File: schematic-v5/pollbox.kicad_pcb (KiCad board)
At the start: 2 copper layers, 50.8 x 74.9 mm, 24 parts, among them P1 CONN_01X15, P10 CONN_01X04, P2 CONN_02X03, P20 CONN_01X04, P3 CONN_01X15, P30 CONN_01X04, P40 CONN_01X04, P50 CONN_01X04, U1 NodeMCU, U2 ULN2803

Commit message: o Completing routing of board v5.
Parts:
- removed W1, W2, W3, W4: TEST_1P, Connect:1pin
- added HOLE1: MountingHole_3.2mm_M3, Mounting_Holes.pretty:MountingHole_3.2mm_M3, F.Cu at (82.5, 52.1)
- added HOLE2: MountingHole_3.2mm_M3, Mounting_Holes.pretty:MountingHole_3.2mm_M3, F.Cu at (123.2, 52.1)
- added HOLE3: MountingHole_3.2mm_M3, Mounting_Holes.pretty:MountingHole_3.2mm_M3, F.Cu at (123.2, 106.7)
- added HOLE4: MountingHole_3.2mm_M3, Mounting_Holes.pretty:MountingHole_3.2mm_M3, F.Cu at (82.5, 106.7)
- U1: value NodeMCU -> NodeMCU_1.0; footprint nodemcu:NodeMCU_wide_2 -> nodemcu:NodeMCU
- U2: footprint Housings_DIP:DIP-18_W7.62mm -> Housings_DIP.pretty:DIP-18_W7.62mm_LongPads
- moved P1 35.7 mm to (121.9, 116.8), turned to 270 degrees
- moved P3 35.6 mm to (121.9, 86.4), turned to 270 degrees
- moved U1 24.4 mm to (105.4, 101.6)
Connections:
- P1 pad 13: (no net) -> Net-(P1-Pad13)
- P1 pad 14: (no net) -> Net-(P1-Pad14)
- P1 pad 5: (no net) -> Net-(P1-Pad5)
- P1 pad 6: (no net) -> Net-(P1-Pad6)
- P3 pad 10: (no net) -> Net-(P3-Pad10)
- P3 pad 3: (no net) -> Net-(P3-Pad3)
- P3 pad 9: (no net) -> Net-(P3-Pad9)
- U1 pad 13: (no net) -> Net-(U1-Pad13)
- U1 pad 14: (no net) -> Net-(U1-Pad14)
- U1 pad 21: (no net) -> Net-(U1-Pad21)
- U1 pad 22: (no net) -> Net-(U1-Pad22)
- U1 pad 28: (no net) -> Net-(U1-Pad28)
- U1 pad 5: (no net) -> Net-(U1-Pad5)
- U1 pad 6: (no net) -> Net-(U1-Pad6)
- U2 pad 11: (no net) -> Net-(U2-Pad11)
- U2 pad 12: (no net) -> Net-(U2-Pad12)
- U2 pad 13: (no net) -> Net-(U2-Pad13)
- U2 pad 6: (no net) -> Net-(U2-Pad6)
- U2 pad 7: (no net) -> Net-(U2-Pad7)
- U2 pad 8: (no net) -> Net-(U2-Pad8)
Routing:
- net (no net): track 73.5 -> 0.00 mm
- net +5V: track 55.9 -> 112.4 mm
- net /SWITCH_4: track 12.9 -> 51.9 mm
- net /SWITCH_5: track 20.3 -> 55.8 mm
- net /SWITCH_3: track 11.5 -> 45.8 mm
- net GND: track 146.8 -> 179.3 mm
- net /SWITCH_2: track 11.8 -> 36.5 mm
- net /LED_5: track 1.27 -> 13.5 mm
- net /LED_2_OUT: track 0.90 -> 11.3 mm
- net /SWITCH_1: track 26.9 -> 36.6 mm
- net /LED_4_OUT: track 8.94 -> 17.1 mm
- net /LED_5_OUT: track 14.0 -> 21.9 mm
- net /LED_1: track 4.49 -> 9.94 mm
- net +3V3: track 159.7 -> 165.1 mm
- net /LED_1_OUT: track 8.26 -> 12.0 mm
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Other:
- net class narrow added: clearance 0.254, trace_width 0.3048, via_dia 0.6, via_drill 0.4

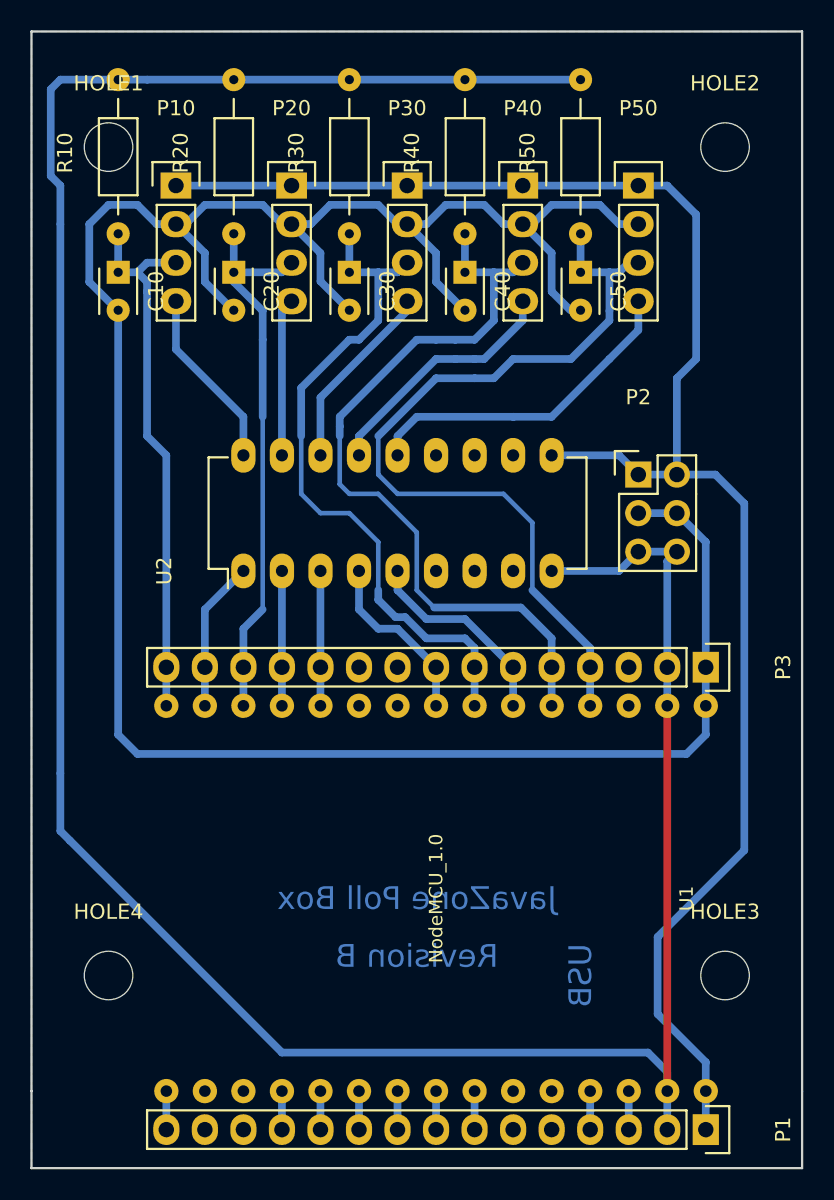
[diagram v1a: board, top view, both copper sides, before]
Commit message: rewire d0 and d1
To enable interrupt on button
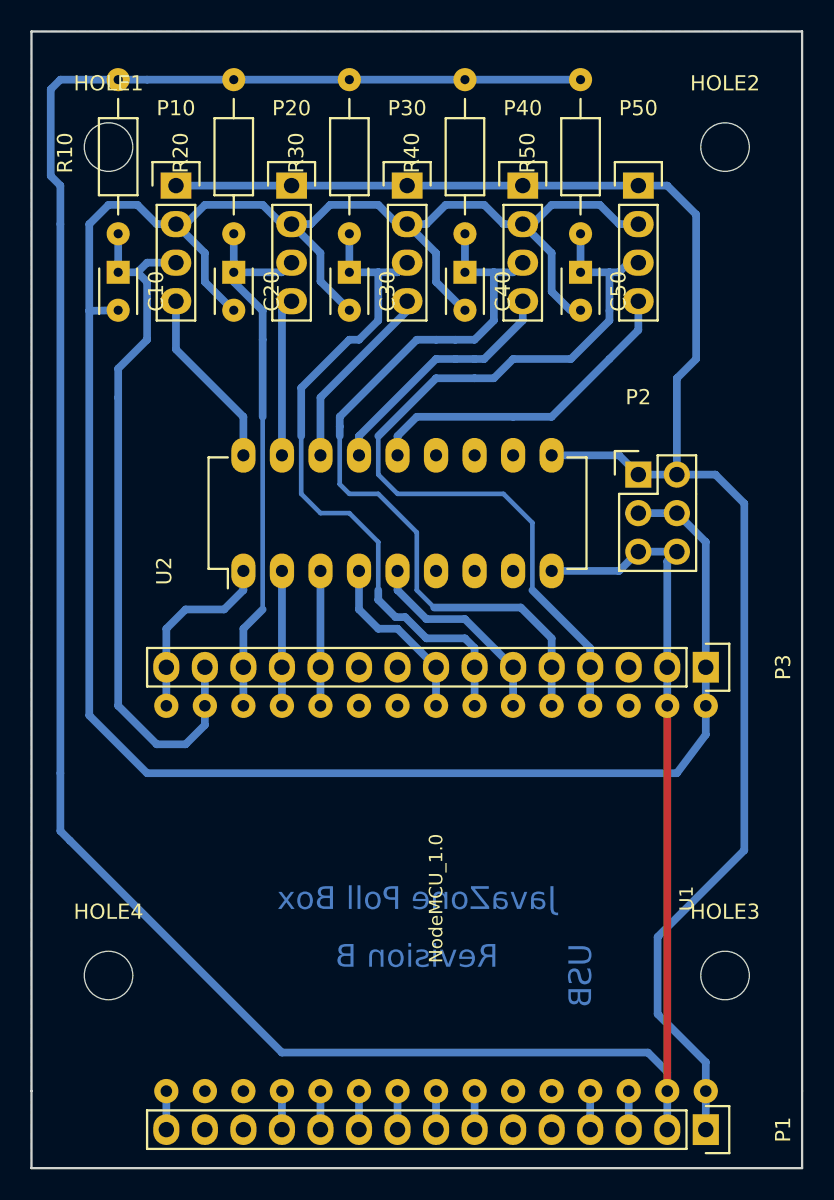
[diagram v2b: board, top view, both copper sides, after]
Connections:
- C10 pad 1: /SWITCH_1 -> /LED_1
- P10 pad 3: /SWITCH_1 -> /LED_1
- P3 pad 15: /SWITCH_1 -> Net-(P3-Pad15)
- R10 pad 1: /SWITCH_1 -> /LED_1
- U1 pad 16: /SWITCH_1 -> Net-(P3-Pad15)
- U2 pad 1: /LED_1 -> Net-(P3-Pad15)
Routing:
- net /LED_1: track 9.94 -> 48.0 mm
- net /SWITCH_1: track 36.6 -> 0.00 mm
- net Net-(P3-Pad15): track 0.00 -> 12.5 mm
- net +3V3: track 165.1 -> 168.6 mm

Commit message: cleanup some tracks
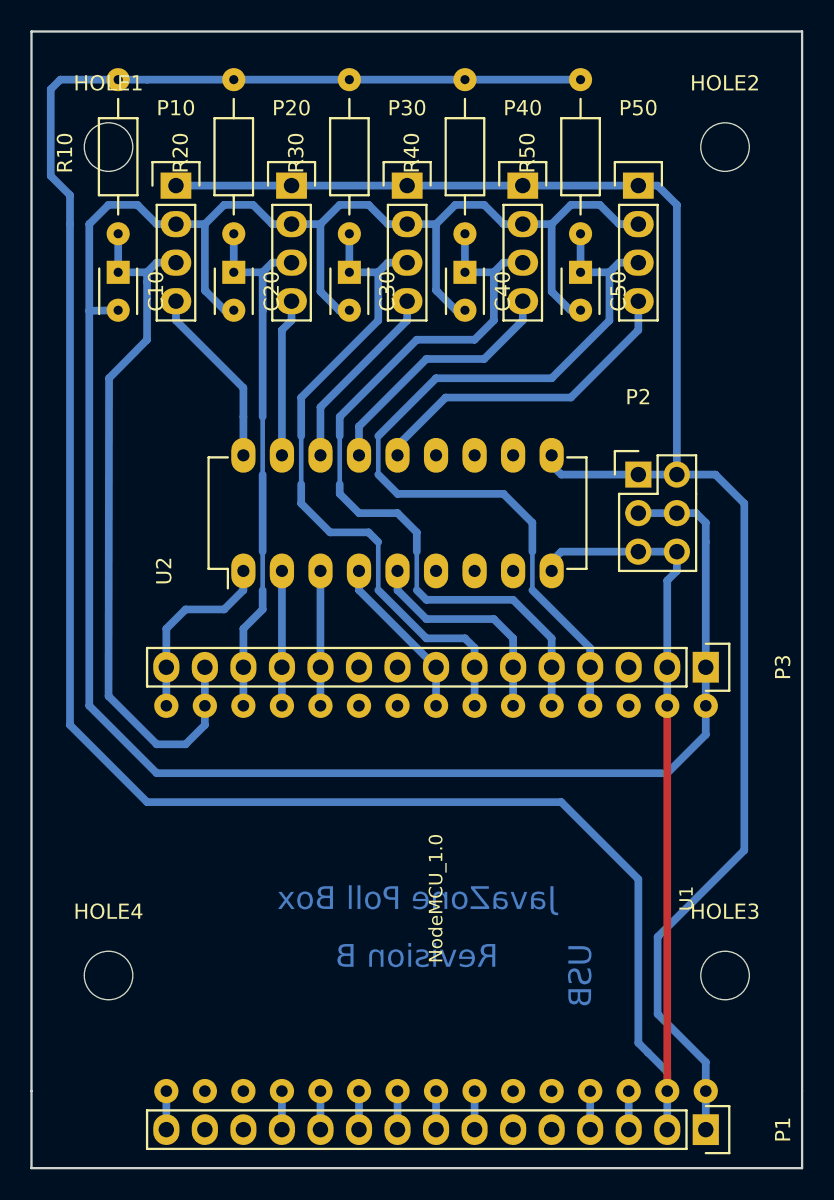
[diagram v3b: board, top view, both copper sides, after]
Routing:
- net GND: track 179.3 -> 181.6 mm
- net /LED_5: track 13.5 -> 14.7 mm
- net +5V: track 112.4 -> 111.3 mm
- net /LED_2_OUT: track 11.3 -> 10.4 mm
- net /SWITCH_2: track 36.5 -> 35.7 mm
- net /LED_4: track 11.7 -> 11.0 mm
- net /LED_3_OUT: track 12.5 -> 13.2 mm
- net /SWITCH_5: track 55.8 -> 56.5 mm
